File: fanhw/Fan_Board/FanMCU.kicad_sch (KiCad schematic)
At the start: 16 parts, among them J2 Conn_01x05_Female, U2 PIC18F26K83-xSP

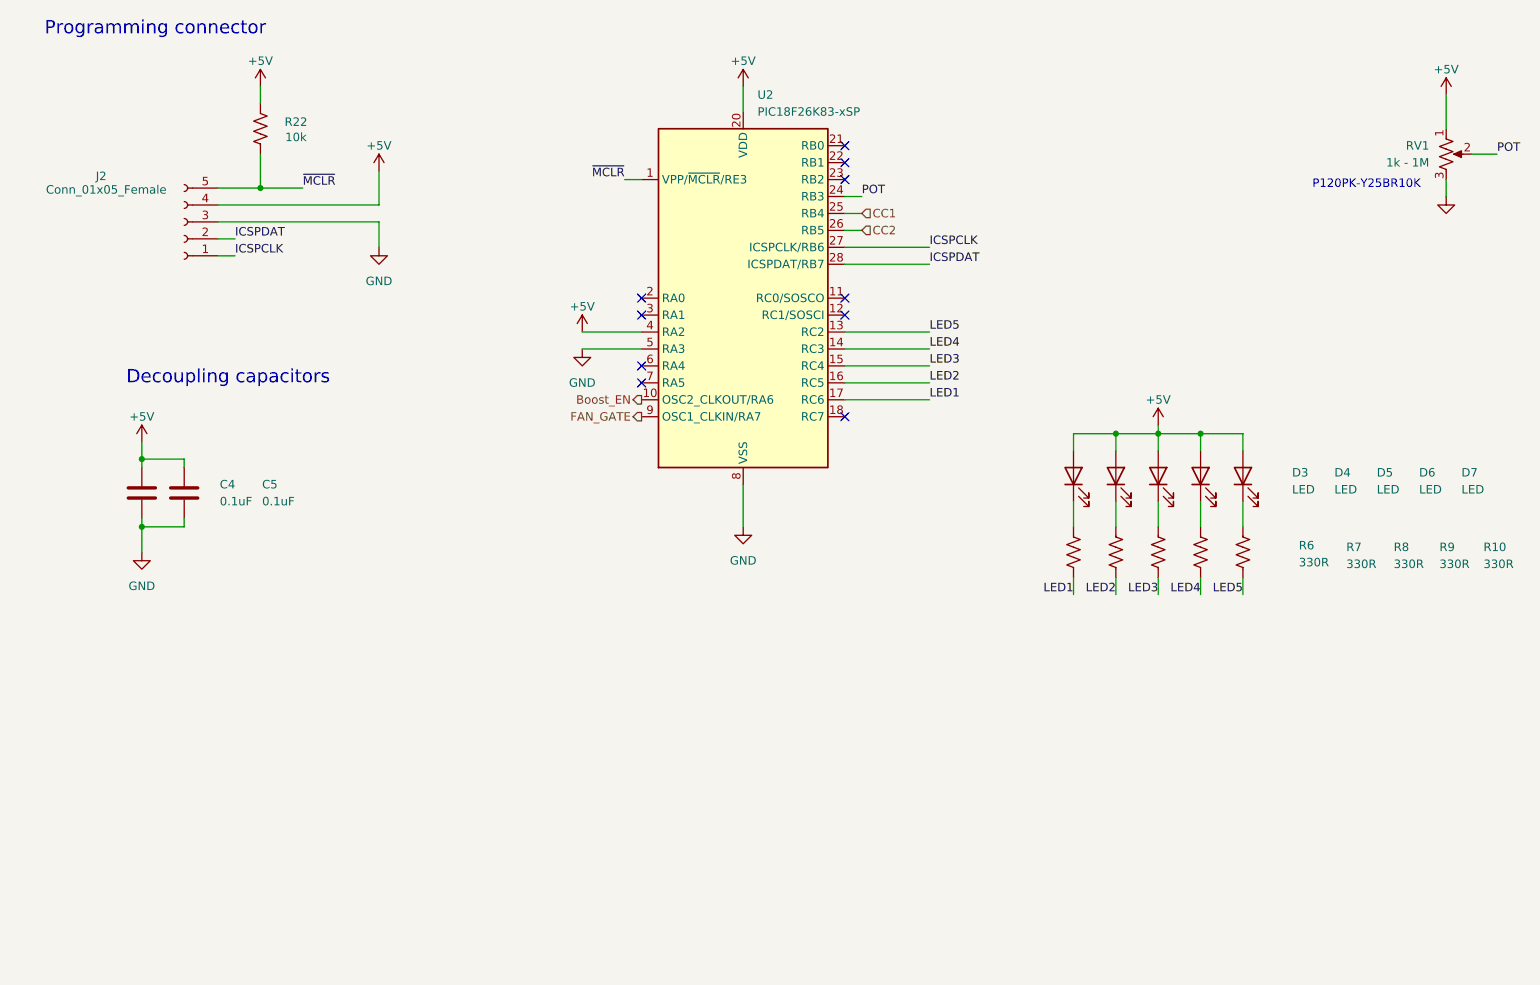
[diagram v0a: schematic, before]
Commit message: added oscillator, regen prod files
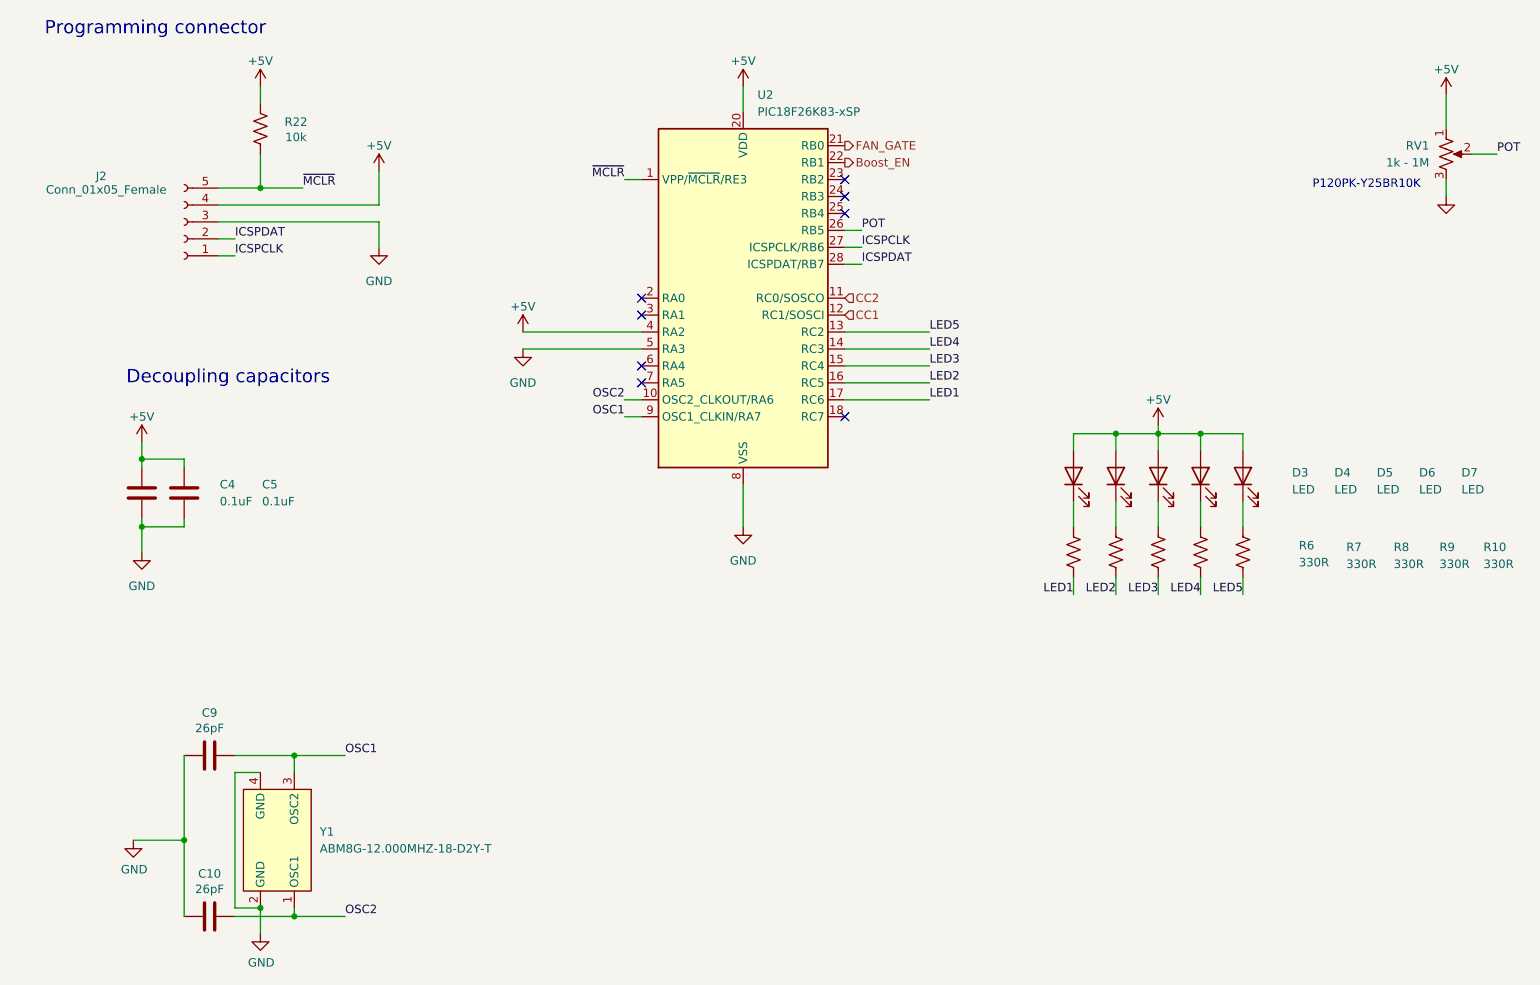
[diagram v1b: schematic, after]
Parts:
- added C10, C9: 26pF, Capacitor_SMD:C_0805_2012Metric_Pad1.18x1.45mm_HandSolder, symbol Device:C
- added Y1: ABM8G-12.000MHZ-18-D2Y-T, Crystal:Crystal_SMD_Abracon_ABM8G-4Pin_3.2x2.5mm, symbol ABM8:ABM8
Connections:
- net Boost_EN: now also U2.22 (RB1); no longer U2.10 (OSC2_CLKOUT/RA6)
- net CC1: now also U2.12 (RC1/SOSCI); no longer U2.25 (RB4)
- net CC2: now also U2.11 (RC0/SOSCO); no longer U2.26 (RB5)
- net FAN_GATE: now also U2.21 (RB0); no longer U2.9 (OSC1_CLKIN/RA7)
- net GND: now also C10.2, C9.2, Y1.2 (GND), Y1.4 (GND)
- net POT: now also U2.26 (RB5); no longer U2.24 (RB3)
- new net OSC1: C9.1, U2.9 (OSC1_CLKIN/RA7), Y1.3 (OSC2)
- new net OSC2: C10.1, U2.10 (OSC2_CLKOUT/RA6), Y1.1 (OSC1)
- no-connect marks 10 -> 8
